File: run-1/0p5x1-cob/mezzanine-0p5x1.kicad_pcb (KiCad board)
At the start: 2 copper layers, 14 x 16 mm, 11 parts

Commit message: Tweaks
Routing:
- net /an_0: track 3.62 -> 5.48 mm

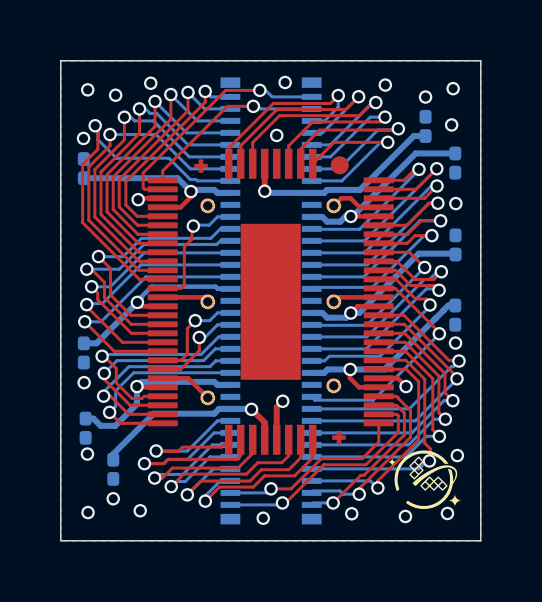
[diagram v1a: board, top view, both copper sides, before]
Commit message: Check symbols against template pad frame
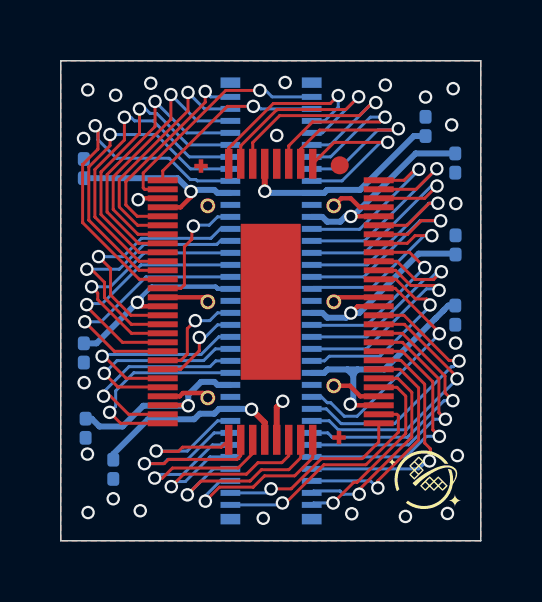
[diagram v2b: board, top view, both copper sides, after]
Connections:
- U102 pad 31: GND -> /bidir_18
- U102 pad 32: VDD_CORE_0 -> /bidir_19
- U102 pad 33: /bidir_18 -> GND
- U102 pad 34: /bidir_19 -> VDD_CORE_0
- U102 pad 47: /bidir_24 -> VDD_IO_2
- U102 pad 48: /bidir_25 -> GND
- U102 pad 49: VDD_IO_2 -> /bidir_24
- U102 pad 50: GND -> /bidir_25
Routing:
- net VDD_IO_2: track 7.35 -> 8.23 mm
- net /bidir_25: track 6.42 -> 7.26 mm
- net /bidir_24: track 5.75 -> 6.39 mm
- net /bidir_18: track 7.46 -> 6.87 mm
- net GND: track 9.85 -> 10.3 mm, vias 25 -> 24
